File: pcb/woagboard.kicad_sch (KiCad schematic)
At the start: 74 parts, among them J10 Flash connection, J2 HRO_TYPE-C-31-M-14, J3 Battery JST, Q2 2N7002, SW16 SW_Push, SW17 SW_Push, SW18 SW_Push, SW19 SW_Push, SW20 SW_Push, SW21 SW_Push, SW22 SW_Push, SW23 SW_Push, SW24 SW_Push, SW25 SW_Push, SW26 SW_Push, SW27 SW_Push, SW28 SW_Push, SW29 SW_Push, SW30 SW_Push, SW31 SW_Push, SW32 SW_Push, SW33 SW_Push, U1 SRV05-4, U10 MAX17048, U3 BQ24075, U9 nRF52840_E73-2G4M08S1C, Y1 32.768 KHz

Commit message: wip: finish left half and start work on right half
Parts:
- removed C17: 100n, Capacitor_SMD:C_0402_1005Metric, symbol Device:C_Small
- removed D16, D17, D18, D19, D20, D21, D22, D23, D24, D25, D26, D27, D28, D29, D30, D31, D32, D33: D, Diode_SMD:D_SOD-523, symbol Device:D_Small
- removed DUSB1: BSD3C051V, Diode_SMD:D_SOD-523, symbol Device:D_TVS
- removed J2: HRO_TYPE-C-31-M-14, Connector_USB:USB_C_Receptacle_HRO_TYPE-C-31-M-12, symbol Connector:USB_C_Receptacle_USB2.0
- removed LED2: orange, LED_SMD:LED_0402_1005Metric, symbol Device:LED_Small
- removed R19: 5k1, Resistor_SMD:R_0402_1005Metric, symbol Device:R_Small
- removed U10: MAX17048, Package_DFN_QFN:DFN-8-1EP_2x2mm_P0.5mm_EP0.7x1.3mm, symbol marbastlib-various:MAX17048
- added C10, C9: 12p, Capacitor_SMD:C_0402_1005Metric, symbol Device:C_Small
- added C2, C3, C8: 4u7, Capacitor_SMD:C_0402_1005Metric, symbol Device:C_Small
- added C4: 1u, Capacitor_SMD:C_0402_1005Metric, symbol Device:C_Small
- added F2: 750 mA, Fuse:Fuse_0603_1608Metric, symbol Device:Fuse_Small
- added J1: Battery JST, Connector_JST:JST_PH_S2B-PH-K_1x02_P2.00mm_Horizontal, symbol Connector_Generic:Conn_01x02
- added J2: Flash connection, Connector_PinHeader_2.54mm:PinHeader_1x05_P2.54mm_Vertical, symbol Connector_Generic:Conn_01x05
- added L4: 10 uH, Inductor_SMD:L_0603_1608Metric, symbol Device:L_Small
- added Q1: 2N7002, Package_TO_SOT_SMD:SOT-23, symbol Transistor_FET:2N7002
- added R14, R15: 10k, Resistor_SMD:R_0402_1005Metric, symbol Device:R_Small
- added R16: 47k, Resistor_SMD:R_0402_1005Metric, symbol Device:R_Small
- added R17: 1k5, Resistor_SMD:R_0402_1005Metric, symbol Device:R_Small
- added R5, R6: 5k1, Resistor_SMD:R_0402_1005Metric, symbol Device:R_Small
- added R8: 100k, Resistor_SMD:R_0402_1005Metric, symbol Device:R_Small
- added RST2: RST, Jumper:SolderJumper-2_P1.3mm_Open_Pad1.0x1.5mm, symbol Switch:SW_Push_45deg
- added SW10, SW11, SW12, SW13, SW14, SW15, SW28, SW3, SW31, SW34, SW35, SW36, SW4, SW5, SW6, SW7, SW8, SW9: SW_Push, PCM_marbastlib-choc:SW_choc_v1_HS_CPG135001S30_1u, symbol Switch:SW_Push_45deg
- added SWPL2: PWR, PCM_marbastlib-various:SW_MSK12C02-HB, symbol Switch:SW_Push_SPDT
- added U2: SRV05-4, Package_TO_SOT_SMD:SOT-23-6, symbol Power_Protection:SRV05-4
- added U4: BQ24075, Package_DFN_QFN:VQFN-16-1EP_3x3mm_P0.5mm_EP1.6x1.6mm, symbol Battery_Management:BQ24075RGT
- added U5: nRF52840_E73-2G4M08S1C, PCM_marbastlib-various:nRF52840_E73-2G4M08S1C, symbol PCM_marbastlib-various:nRF52840_E73-2G4M08S1C
- added USB1, USB2: TYPE-C 16PIN 2MD(073), easyeda2kicad:USB-C-SMD_TYPE-C-6PIN-2MD-073, symbol easyeda2kicad:TYPE-C16PIN2MD(073)
- added WOAG1, WOAG2: SHIELDNET, Jumper:SolderJumper-2_P1.3mm_Bridged2Bar_RoundedPad1.0x1.5mm, symbol Device:R_Small
- added Y2: 32.768 KHz, Crystal:Crystal_SMD_2012-2Pin_2.0x1.2mm, symbol Device:Crystal_Small
- C1: value 100n -> 4u7
- J3: footprint Connector_JST:JST_PH_S2B-PH-SM4-TB_1x02-1MP_P2.00mm_Horizontal -> Connector_JST:JST_PH_S2B-PH-K_1x02_P2.00mm_Horizontal
- R10: value 1k5 -> 100R
- R18: value 5k1 -> 3k9
- RST1: renamed from SWRST1; footprint PCM_marbastlib-various:SW_SPST_SKQG_WithStem -> Jumper:SolderJumper-2_P1.3mm_Open_Pad1.0x1.5mm
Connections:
- net +3.3V: now also C4.1, J2.5 (Pin_5), L4.2, U5.19 (VDD); no longer R18.2
- net +5V: now also C1.1, R10.1, C8.1, F2.2, U2.5 (VP), U4.13 (IN), U5.27 (VBUS)
- net +BATT: now also C3.1, J1.1 (Pin_1), R8.2, U4.2 (BAT), U4.3 (BAT)
- net +VSW: now also C2.1, U4.10 (OUT), U4.11 (OUT), U4.6 (EN1), U5.23 (VDDH)
- net GND: now also R1.2, R18.2, R2.1, SW16.2, SW17.2, SW18.2, SW19.2, SW20.2, SW21.2, SW22.2, SW23.2, SW24.2, SW25.2, SW26.2, SW27.2, SW28.2, SW29.2, SW30.2, SW31.2, SW32.2, SW33.2, C10.2, C2.2, C3.2, C4.2, C8.2, C9.2, J1.2 (Pin_2), J2.4 (Pin_4), Q1.2 (S), R14.2, R15.2, R16.2, R17.2, R5.1, R6.2, RST2.2, SW10.2, SW11.2, SW12.2, SW13.2, SW14.2, SW15.2, SW28.2, SW3.2, SW31.2, SW34.2, SW35.2, SW36.2, SW4.2, SW5.2, SW6.2, SW7.2, SW8.2, SW9.2, SWPL2.3 (C), SWPL2.MP, U2.2 (VN), U4.17 (VSS), U4.4 (~{CE}), U4.5 (EN2), U4.8 (VSS), U5.21 (GND), U5.24 (GND), U5.5 (GND), USB1.1 (GND), USB1.12 (GND), USB2.1 (GND), USB2.12 (GND), WOAG1.2, WOAG2.2; no longer L2.2
- net ILIM: now also R17.1, U4.12 (ILIM)
- net TMR: now also R16.1, U4.14 (TMR)
- net USB-D+: now also USB1.6 (DP1), USB1.8 (DP2)
- net USB-D-: now also USB1.5 (DN2), USB1.7 (DN1)
- net VBUS: now also L2.1, USB1.11 (VBUS), USB1.2 (VBUS), USB2.11 (VBUS), USB2.2 (VBUS)
- net Switch1: now reaches U9.10 (P0.30/AIN6)
- net Switch1: now also SW28.1
- net Switch6: now reaches U9.12 (P0.26)
- net Switch6: now also SW6.1
- net Switch7: now reaches U9.14 (P0.06)
- net Switch7: now also SW7.1
- net Switch8: now reaches U9.16 (P0.08)
- net Switch8: now also SW8.1
- net Switch10: now reaches U9.20 (P0.12)
- net Switch10: now also SW10.1
- net Switch12: now reaches U9.28 (P0.15)
- net Switch12: now also SW12.1
- net Switch13: now reaches U9.30 (P0.17)
- net Switch13: now also SW13.1
- net Switch14: now reaches U9.32 (P0.20)
- net Switch14: now also SW14.1
- net Switch16: now reaches U9.33 (P0.13)
- net Switch16: now also SW16.1
- net Switch18: now reaches U9.35 (P0.24)
- net Switch18: now also SW18.1
- net Switch5: now reaches U9.6 (P1.13)
- net Switch5: now also SW5.1
- net Switch2: now reaches U9.9 (P0.31/AIN7)
- net Switch2: now also SW31.1
- net at R2.2: now also USB1.4 (CC1)
- net at R10.2: now also Q1.1 (G), R14.1; no longer U3.9 (~{CHG})
- removed net C0: SW16.1, SW21.1, SW26.1, U9.7 (P0.02/AIN0)
- removed net C1: SW17.1, SW22.1, SW27.1, U9.3 (P0.03/AIN1)
- removed net C2: SW18.1, SW23.1, SW28.1, SW31.1, U9.18 (P0.04/AIN2)
- removed net C3: SW19.1, SW24.1, SW29.1, SW32.1, U9.4 (P0.28/AIN4)
- removed net C4: SW20.1, SW25.1, SW30.1, SW33.1, U9.8 (P0.29/AIN5)
- removed net Earth: C1.1, L2.1
- net GNDPWR: no longer names the net of R1.1
- net GNDPWR: now also USB1.10 (CC2); no longer R2.1
- net R0: no longer names the net of U9.38 (P1.02)
- net R1: no longer names the net of U9.40 (P1.04)
- net R2: no longer names the net of U9.42 (P1.06)
- net R3: no longer names the net of U9.17 (P1.09)
- net SCL: no longer names the net of U9.15 (P0.05/AIN3)
- net SDA: no longer names the net of R18.1
- net SDA: now also U4.16 (ISET); no longer U9.22 (P0.07)
- net UG_EN renamed Switch17
- net Switch17: now also SW17.1
- net UG_LV renamed Switch15
- net Switch15: now also SW15.1
- new net: F2.1, L2.2
- new net: USB2.13 (SHELL), USB2.14 (SHELL), WOAG2.1
- new net: R8.1, SWPL2.1 (A)
- new net: C10.1, U5.13 (P0.01/XL2), Y2.1
- new net: USB1.13 (SHELL), USB1.14 (SHELL), WOAG1.1
- new net: C9.1, U5.11 (P0.00/XL1), Y2.2
- new net: R6.1, USB2.10 (CC2)
- new net: R5.2, USB2.4 (CC1)
- new net: R15.1, U4.1 (TS)
- new net DCCH-R: L4.1, U5.25 (DCCH)
- new net RST-R: J2.3 (Pin_3), RST2.1, U5.26 (P0.18/~{RESET})
- new net SWDCLK-R: J2.1 (Pin_1), U5.39 (SWDCLK)
- new net SWDIO-R: J2.2 (Pin_2), U5.37 (SWDIO)
- new net SYSOFF-R: Q1.3 (D), SWPL2.2 (B), U4.15 (SYSOFF)
- new net Switch11: SW11.1, U9.22 (P0.07)
- new net Switch19: SW19.1, U5.10 (P0.30/AIN6)
- new net Switch20: SW20.1, U5.9 (P0.31/AIN7)
- new net Switch21: SW21.1, U5.8 (P0.29/AIN5)
- new net Switch22: SW22.1, U5.7 (P0.02/AIN0)
- new net Switch23: SW23.1, U5.6 (P1.13)
- new net Switch24: SW24.1, U5.12 (P0.26)
- new net Switch25: SW25.1, U5.14 (P0.06)
- new net Switch26: SW26.1, U5.16 (P0.08)
- new net Switch27: SW27.1, U5.18 (P0.04/AIN2)
- new net Switch28: SW28.1, U5.20 (P0.12)
- new net Switch29: SW29.1, U5.22 (P0.07)
- new net Switch3: SW3.1, U9.8 (P0.29/AIN5)
- new net Switch30: SW30.1, U5.28 (P0.15)
- new net Switch31: SW31.1, U5.30 (P0.17)
- new net Switch32: SW32.1, U5.32 (P0.20)
- new net Switch33: SW33.1, U5.34 (P0.22)
- new net Switch34: SW34.1, U5.33 (P0.13)
- new net Switch35: SW35.1, U5.36 (P1.00)
- new net Switch36: SW36.1, U5.35 (P0.24)
- new net Switch4: SW4.1, U9.7 (P0.02/AIN0)
- new net Switch9: SW9.1, U9.18 (P0.04/AIN2)
- new net USB-R-D+: U2.6 (IO4), U5.31 (D+), USB2.6 (DP1), USB2.8 (DP2)
- new net USB-R-D-: U2.1 (IO1), U5.29 (D-), USB2.5 (DN2), USB2.7 (DN1)
- no-connect marks 21 -> 34
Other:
- note removed: "Voltage sensing (advanced)"
- moved on the sheet: C15, C16, SW28, SW31, Y1

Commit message: wip: initial pcb of full woagboard
note: Do not print this. It's not even close to ready probably
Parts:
- removed Q1, Q2: 2N7002, Package_TO_SOT_SMD:SOT-23, symbol Transistor_FET:2N7002
- removed R10: 100R, Resistor_SMD:R_0402_1005Metric, symbol Device:R_Small
- removed R14, R7: 10k, Resistor_SMD:R_0402_1005Metric, symbol Device:R_Small
- removed R8: 100k, Resistor_SMD:R_0402_1005Metric, symbol Device:R_Small
- removed RST1, RST2: RST, Jumper:SolderJumper-2_P1.3mm_Open_Pad1.0x1.5mm, symbol Switch:SW_Push_45deg
- removed SWPL1, SWPL2: PWR, PCM_marbastlib-various:SW_MSK12C02-HB, symbol Switch:SW_Push_SPDT
- added LED1, LED2: Orange, LED_SMD:LED_0805_2012Metric, symbol Device:LED_Small
- added RST1, RST2: EVQ-P7C01P, EVQ-P7C01P:SW_EVQ-P7C01P, symbol EVQ-P7C01P:EVQ-P7C01P
- R13, R18: footprint Resistor_SMD:R_0402_1005Metric -> Resistor_SMD:R_0603_1608Metric
- R3: value 100k -> 1k5
- R4: value 100R -> 1k5
- renumbered J10 to J4
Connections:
- net +5V: no longer R4.1
- net +BATT: no longer R3.2
- net +VSW: now also LED1.2 (A), LED2.2 (A)
- net GND: now also RST1.2_1, RST1.2_2, RST2.2_1, RST2.2_2
- net RST: now also RST1.1_1, RST1.1_2
- net RST-R: now also RST2.1_1, RST2.1_2
- net Switch19: now also U5.34 (P0.22); no longer U5.10 (P0.30/AIN6)
- net Switch20: now also U5.32 (P0.20); no longer U5.9 (P0.31/AIN7)
- net Switch21: now also U5.30 (P0.17); no longer U5.8 (P0.29/AIN5)
- net Switch22: now also U5.28 (P0.15); no longer U5.7 (P0.02/AIN0)
- net Switch23: now also U5.22 (P0.07); no longer U5.6 (P1.13)
- net Switch24: now also U5.9 (P0.31/AIN7); no longer U5.12 (P0.26)
- net Switch29: now also U5.10 (P0.30/AIN6); no longer U5.22 (P0.07)
- net Switch30: now also U5.12 (P0.26); no longer U5.28 (P0.15)
- net Switch31: now also U5.8 (P0.29/AIN5); no longer U5.30 (P0.17)
- net Switch32: now also U5.7 (P0.02/AIN0); no longer U5.32 (P0.20)
- net Switch33: now also U5.6 (P1.13); no longer U5.34 (P0.22)
- net Switch34: now also U5.4 (P0.28/AIN4); no longer U5.33 (P0.13)
- net Switch35: now also U5.3 (P0.03/AIN1); no longer U5.36 (P1.00)
- net Switch36: now also U5.2 (P1.10); no longer U5.35 (P0.24)
- net at U3.9 (~{CHG}): now also R3.2
- net at R4.2: now also U4.9 (~{CHG})
- net at R3.1: now also LED1.1 (K)
- net SYSOFF: no longer names the net of U3.15 (SYSOFF)
- net SYSOFF-R: no longer names the net of U4.15 (SYSOFF)
- new net: LED2.1 (K), R4.1
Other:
- note removed: "SYSOFF 1 (SW1 pos 1): Batt OFF SYSOFF 0 (SW1 pos 3): Batt ON"

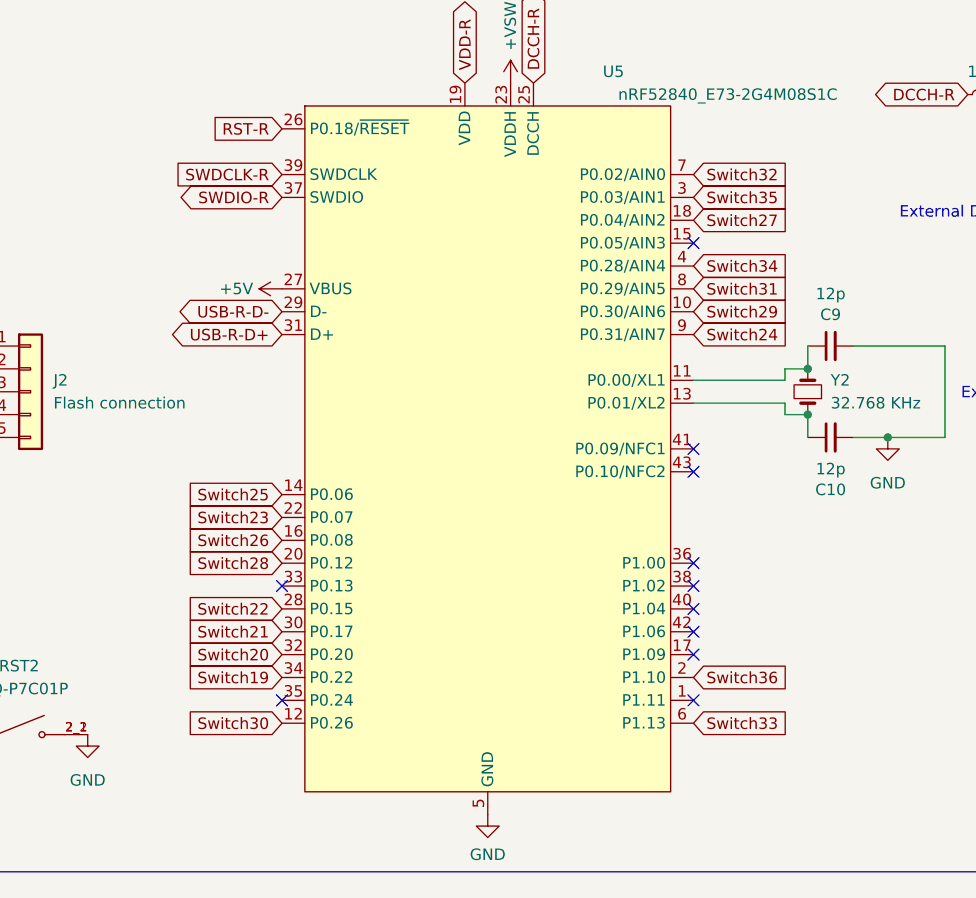
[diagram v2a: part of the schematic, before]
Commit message: fix: much better routing
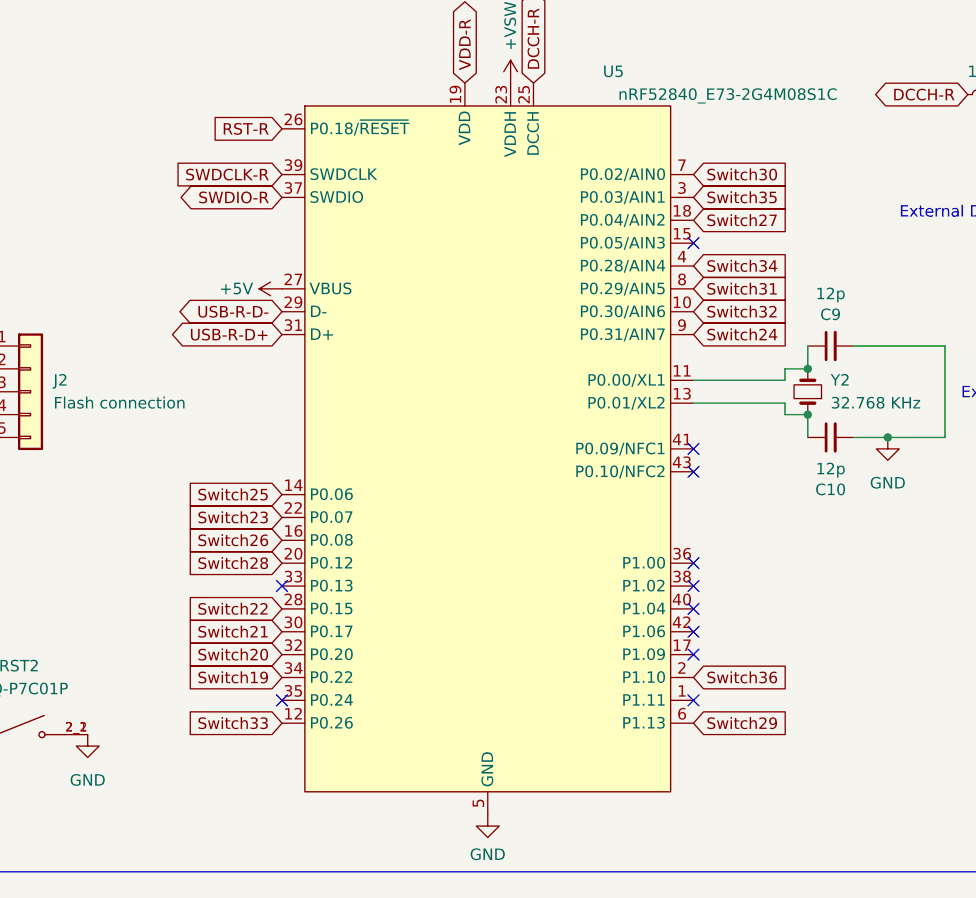
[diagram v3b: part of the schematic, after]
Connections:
- net Switch29: now also U5.6 (P1.13); no longer U5.10 (P0.30/AIN6)
- net Switch30: now also U5.7 (P0.02/AIN0); no longer U5.12 (P0.26)
- net Switch32: now also U5.10 (P0.30/AIN6); no longer U5.7 (P0.02/AIN0)
- net Switch33: now also U5.12 (P0.26); no longer U5.6 (P1.13)

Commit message: feat: RC1
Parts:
- U3, U4: footprint Package_DFN_QFN:VQFN-16-1EP_3x3mm_P0.5mm_EP1.6x1.6mm -> SamacSys_Parts:QFN50P300X300X80-17N-D

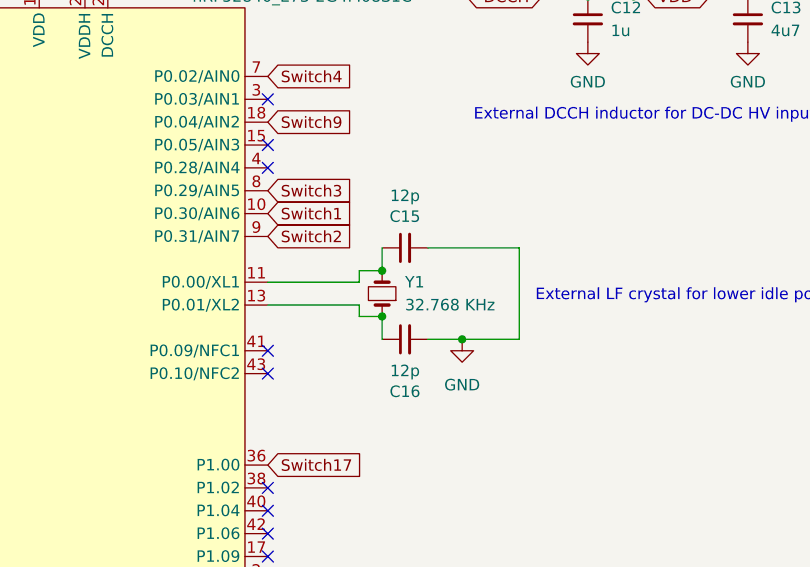
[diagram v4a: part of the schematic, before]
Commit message: pcb: replace oscillator
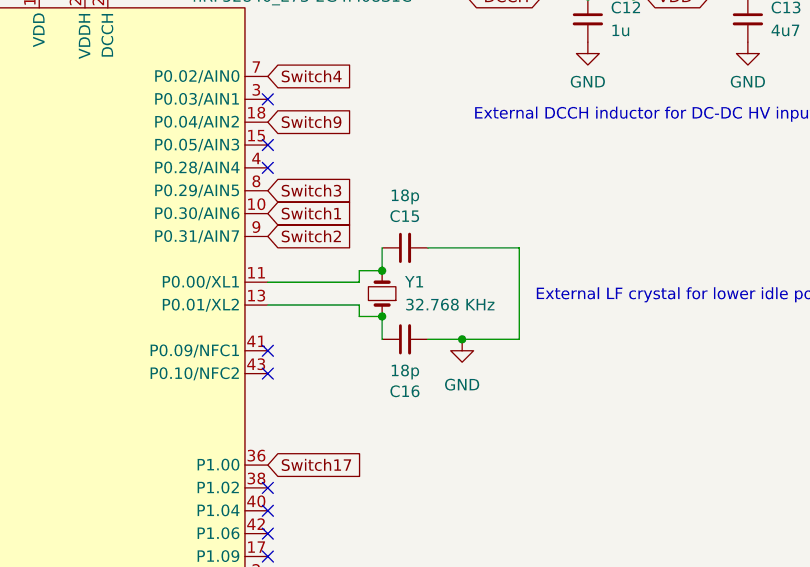
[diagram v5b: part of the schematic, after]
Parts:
- C15, C16: value 12p -> 18p
- Y1, Y2: footprint Crystal:Crystal_SMD_2012-2Pin_2.0x1.2mm -> Library:Q13FC13500004

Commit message: wip(pcb): heavy wip on woagboard v0.2
- new usb port
- redoing routing again
- soldering + hotswap in one
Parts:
- removed USB1, USB2: TYPE-C 16PIN 2MD(073), easyeda2kicad:USB-C-SMD_TYPE-C-6PIN-2MD-073, symbol easyeda2kicad:TYPE-C16PIN2MD(073)
- added USB1, USB2: HRO_TYPE-C-31-M-14, PCM_marbastlib-various:USB_C_Receptacle_HRO_TYPE-C-31-M-12, symbol Connector:USB_C_Receptacle_USB2.0
- SW10, SW11, SW12, SW13, SW14, SW15, SW16, SW17, SW18, SW19, SW20, SW21, SW22, SW23, SW24, SW25, SW26, SW27, SW28, SW29, SW3, SW30, SW31, SW32, SW33, SW34, SW35, SW36, SW4, SW5, SW6, SW7, SW8, SW9: footprint PCM_marbastlib-choc:SW_choc_v1_HS_CPG135001S30_1u -> Library:SW_choc_v1_HS_Solder; now left out of the parts list
- U1, U2: value SRV05-4 -> USBLC6-2; symbol Power_Protection:SRV05-4 -> Power_Protection:USBLC6-2SC6
- WOAG1, WOAG2: now left out of the parts list
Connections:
- net +3.3V: no longer C4.1, J2.5 (Pin_5), L4.2, U5.19 (VDD)
- net +5V: no longer C1.1, C8.1, F2.2, U2.5 (VP), U4.13 (IN), U5.27 (VBUS)
- net +BATT: no longer C3.1, J1.1 (Pin_1), U4.2 (BAT), U4.3 (BAT)
- net +VSW: no longer C2.1, LED2.2 (A), U4.10 (OUT), U4.11 (OUT), U4.6 (EN1), U5.23 (VDDH)
- net GND: now also R2.2, R6.1, USB1.A1 (GND), USB1.A12 (GND), USB1.B1 (GND), USB1.B12 (GND), USB2.A1 (GND), USB2.A12 (GND), USB2.B1 (GND), USB2.B12 (GND); no longer R2.1, R6.2
- net ILIM: no longer R17.1, U4.12 (ILIM)
- net Switch16: now also U9.36 (P1.00); no longer U9.33 (P0.13)
- net Switch17: now also U9.33 (P0.13); no longer U9.36 (P1.00)
- net TMR: no longer R16.1, U4.14 (TMR)
- net USB-D+: now also U1.1 (I/O1); no longer U1.6 (IO4)
- net USB-D-: now also U1.3 (I/O2); no longer U1.1 (IO1)
- net USB-R-D+: now also U2.1 (I/O1); no longer U2.6 (IO4)
- net USB-R-D-: now also U2.3 (I/O2); no longer U2.1 (IO1)
- net VBUS: now also USB1.A4 (VBUS), USB1.A9 (VBUS), USB1.B4 (VBUS), USB1.B9 (VBUS); no longer L2.1
- net at WOAG2.1: now also USB2.S1 (SHIELD)
- net at R1.1: now also USB1.A5 (CC1)
- net at WOAG1.1: now also USB1.S1 (SHIELD)
- net at R5.2: now also USB2.A5 (CC1)
- net USB-Din-: now reaches U1.4 (I/O2)
- net USB-Din-: now also USB1.A7 (D-), USB1.B7 (D-)
- net USB-R-Din-: now reaches U2.4 (I/O2)
- net USB-R-Din-: now also USB2.A7 (D-), USB2.B7 (D-)
- new net: R2.1, USB1.B5 (CC2)
- new net: R6.2, USB2.B5 (CC2)
- new net +3.3V-R: C4.1, J2.5 (Pin_5), L4.2, U5.19 (VDD)
- new net +5V-R: C1.1, C8.1, F2.2, U2.5 (VBUS), U4.13 (IN), U5.27 (VBUS)
- new net +BATT-R: C3.1, J1.1 (Pin_1), U4.2 (BAT), U4.3 (BAT)
- new net +VSW-R: C2.1, LED2.2 (A), U4.10 (OUT), U4.11 (OUT), U4.6 (EN1), U5.23 (VDDH)
- new net ILIM-R: R17.1, U4.12 (ILIM)
- new net TMR-R: R16.1, U4.14 (TMR)
- new net USB-Din+: U1.6 (I/O1), USB1.A6 (D+), USB1.B6 (D+)
- new net USB-R-Din+: U2.6 (I/O1), USB2.A6 (D+), USB2.B6 (D+)
- new net VBUS-R: L2.1, USB2.A4 (VBUS), USB2.A9 (VBUS), USB2.B4 (VBUS), USB2.B9 (VBUS)
- no-connect marks 34 -> 30

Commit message: feat: woagboard V0.2 REV1
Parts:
- removed RST1, RST2: EVQ-P7C01P, EVQ-P7C01P:SW_EVQ-P7C01P, symbol EVQ-P7C01P:EVQ-P7C01P
- added LED3, LED4: Yellow, LED_SMD:LED_0805_2012Metric, symbol Device:LED_Small
- added RST1, RST2: EVQ-P7C01P, Library:EVQ-P7C, symbol Switch:SW_Push_45deg
- SW10, SW11, SW12, SW13, SW14, SW15, SW16, SW17, SW18, SW19, SW20, SW21, SW22, SW23, SW24, SW25, SW26, SW27, SW28, SW29, SW3, SW30, SW31, SW32, SW33, SW34, SW35, SW36, SW4, SW5, SW6, SW7, SW8, SW9: footprint Library:SW_choc_v1_HS_Solder -> Library:SW_choc_v1_HS_No_LED
- U3, U4: footprint SamacSys_Parts:QFN50P300X300X80-17N-D -> Package_DFN_QFN:VQFN-16-1EP_3x3mm_P0.5mm_EP1.68x1.68mm
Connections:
- net +3.3V: now also J4.3 (Pin_3); no longer J4.5 (Pin_5)
- net +3.3V-R: now also J2.3 (Pin_3); no longer J2.5 (Pin_5)
- net GND: now also J2.5 (Pin_5), J4.5 (Pin_5), LED3.2 (A), LED4.1 (K), RST1.2, RST2.2; no longer J2.4 (Pin_4), J4.4 (Pin_4)
- net RST: now also J4.4 (Pin_4), RST1.1; no longer J4.3 (Pin_3)
- net RST-R: now also J2.4 (Pin_4), RST2.1; no longer J2.3 (Pin_3)
- net Switch19: now also U5.36 (P1.00); no longer U5.34 (P0.22)
- net Switch20: now also U5.34 (P0.22); no longer U5.32 (P0.20)
- net Switch21: now also U5.32 (P0.20); no longer U5.30 (P0.17)
- net Switch22: now also U5.30 (P0.17); no longer U5.28 (P0.15)
- net Switch23: now also U5.28 (P0.15); no longer U5.22 (P0.07)
- net Switch24: now also U5.12 (P0.26); no longer U5.9 (P0.31/AIN7)
- net Switch25: now also U5.20 (P0.12); no longer U5.14 (P0.06)
- net Switch26: now also U5.18 (P0.04/AIN2); no longer U5.16 (P0.08)
- net Switch27: now also U5.16 (P0.08); no longer U5.18 (P0.04/AIN2)
- net Switch28: now also U5.14 (P0.06); no longer U5.20 (P0.12)
- net Switch32: now also U5.9 (P0.31/AIN7); no longer U5.10 (P0.30/AIN6)
- net Switch33: now also U5.10 (P0.30/AIN6); no longer U5.12 (P0.26)
- net Switch6: now also U9.18 (P0.04/AIN2); no longer U9.12 (P0.26)
- net Switch7: now also U9.16 (P0.08); no longer U9.14 (P0.06)
- net Switch8: now also U9.12 (P0.26); no longer U9.16 (P0.08)
- net Switch9: now also U9.14 (P0.06); no longer U9.18 (P0.04/AIN2)
- net at U9.4 (P0.28/AIN4): now also LED3.1 (K)
- net at U5.33 (P0.13): now also LED4.2 (A)
- no-connect marks 30 -> 28
